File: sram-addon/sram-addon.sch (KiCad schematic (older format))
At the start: 10 parts, among them J1 Conn_01x02_Male, J10 Conn_01x12_Male, J12 Conn_01x15_Male, J7 Conn_01x09_Male, J8 Conn_01x06_Male, U1 CY62167EV18

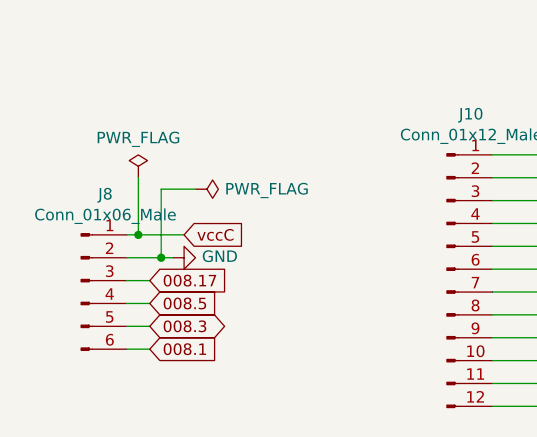
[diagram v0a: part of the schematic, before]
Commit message: sram-addon: update header
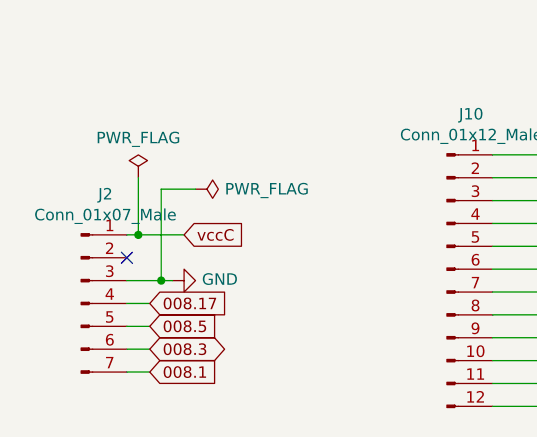
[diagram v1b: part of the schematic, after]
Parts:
- removed J8: Conn_01x06_Male, Connector_PinHeader_2.54mm:PinHeader_1x06_P2.54mm_Vertical, symbol Connector:Conn_01x06_Male
- added J2: Conn_01x07_Male, Connector_PinHeader_2.54mm:PinHeader_1x07_P2.54mm_Vertical, symbol Connector:Conn_01x07_Male
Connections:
- net 008.1: now also J2.7 (Pin_7)
- net 008.17: now also J2.4 (Pin_4)
- net 008.3: now also J2.6 (Pin_6)
- net 008.5: now also J2.5 (Pin_5)
- net GND: now also J2.3 (Pin_3)
- net vccC: now also J2.1 (Pin_1)
- no-connect marks 0 -> 1
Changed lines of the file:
@@
 Wire Wire Line
 	6000 6500 5800 6500
-Text GLabel 1900 6250 2    50   Input ~ 0
+Text GLabel 1900 6350 2    50   Input ~ 0
 008.17
-Text GLabel 1900 6350 2    50   Input ~ 0
+Text GLabel 1900 6450 2    50   Input ~ 0
 008.5
-Text GLabel 1900 6450 2    50   BiDi ~ 0
+Text GLabel 1900 6550 2    50   BiDi ~ 0
 008.3
-Text GLabel 1900 6550 2    50   Input ~ 0
+Text GLabel 1900 6650 2    50   Input ~ 0
 008.1
 Text GLabel 2050 6050 2    50   Input ~ 0
@@
 L power:GND #PWR05
 U 1 1 5C523692
-P 2000 6150
-F 0 "#PWR05" H 2000 5900 50  0001 C CNN
-F 1 "GND" V 2005 6022 50  0000 R CNN
-F 2 "" H 2000 6150 50  0001 C CNN
-F 3 "" H 2000 6150 50  0001 C CNN
-	1    2000 6150
+P 2000 6250
+F 0 "#PWR05" H 2000 6000 50  0001 C CNN
+F 1 "GND" V 2005 6122 50  0000 R CNN
+F 2 "" H 2000 6250 50  0001 C CNN
+F 3 "" H 2000 6250 50  0001 C CNN
+	1    2000 6250
 	0    -1   -1   0
 $EndComp
@@
 	1    0    0    -1
 $EndComp
-$Comp
-L Connector:Conn_01x06_Male J8
-U 1 1 5C6C1C0B
-P 1600 6250
-F 0 "J8" H 1706 6628 50  0000 C CNN
-F 1 "Conn_01x06_Male" H 1706 6537 50  0000 C CNN
-F 2 "Connector_PinHeader_2.54mm:PinHeader_1x06_P2.54mm_Vertical" H 1600 6250 50  0001 C CNN
-F 3 "~" H 1600 6250 50  0001 C CNN
-	1    1600 6250
-	1    0    0    -1
-$EndComp
 Wire Wire Line
 	1800 6050 1850 6050
 Wire Wire Line
-	1800 6250 1900 6250
-Wire Wire Line
 	1800 6350 1900 6350
 Wire Wire Line
@@
 Wire Wire Line
 	1800 6550 1900 6550
+Wire Wire Line
+	1800 6650 1900 6650
 Wire Wire Line
 	3400 5700 3600 5700
@@
 	1850 6050 2050 6050
 Wire Wire Line
-	1800 6150 1950 6150
+	1800 6250 1950 6250
 Wire Wire Line
 	2100 5850 1950 5850
-Wire Wire Line
-	1950 5850 1950 6150
-Connection ~ 1950 6150
-Wire Wire Line
-	1950 6150 2000 6150
+Connection ~ 1950 6250
+Wire Wire Line
+	1950 6250 2000 6250
 Wire Wire Line
 	5100 3300 5350 3300
@@
 	1    0    0    -1
 $EndComp
+$Comp
+L Connector:Conn_01x07_Male J2
+U 1 1 5C2E58F7
+P 1600 6350
+F 0 "J2" H 1706 6828 50  0000 C CNN
+F 1 "Conn_01x07_Male" H 1706 6737 50  0000 C CNN
+F 2 "Connector_PinHeader_2.54mm:PinHeader_1x07_P2.54mm_Vertical" H 1600 6350 50  0001 C CNN
+F 3 "~" H 1600 6350 50  0001 C CNN
+	1    1600 6350
+	1    0    0    -1
+$EndComp
+Wire Wire Line
+	1950 5850 1950 6250
+NoConn ~ 1800 6150
 $EndSCHEMATC
